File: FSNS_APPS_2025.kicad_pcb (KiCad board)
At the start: 2 copper layers, 59 parts, among them K1 PR12-12V-360-1A, Q1 NDT3055L, U1 STM32F103C8T6, U2 MCP6001-OT, U3 MCP6001-OT, U4 LM1117-Q1, U5 LM1117-Q1, U6 LM1117-Q1, U7 TCAN3404-Q1, U8 LM1117-Q1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

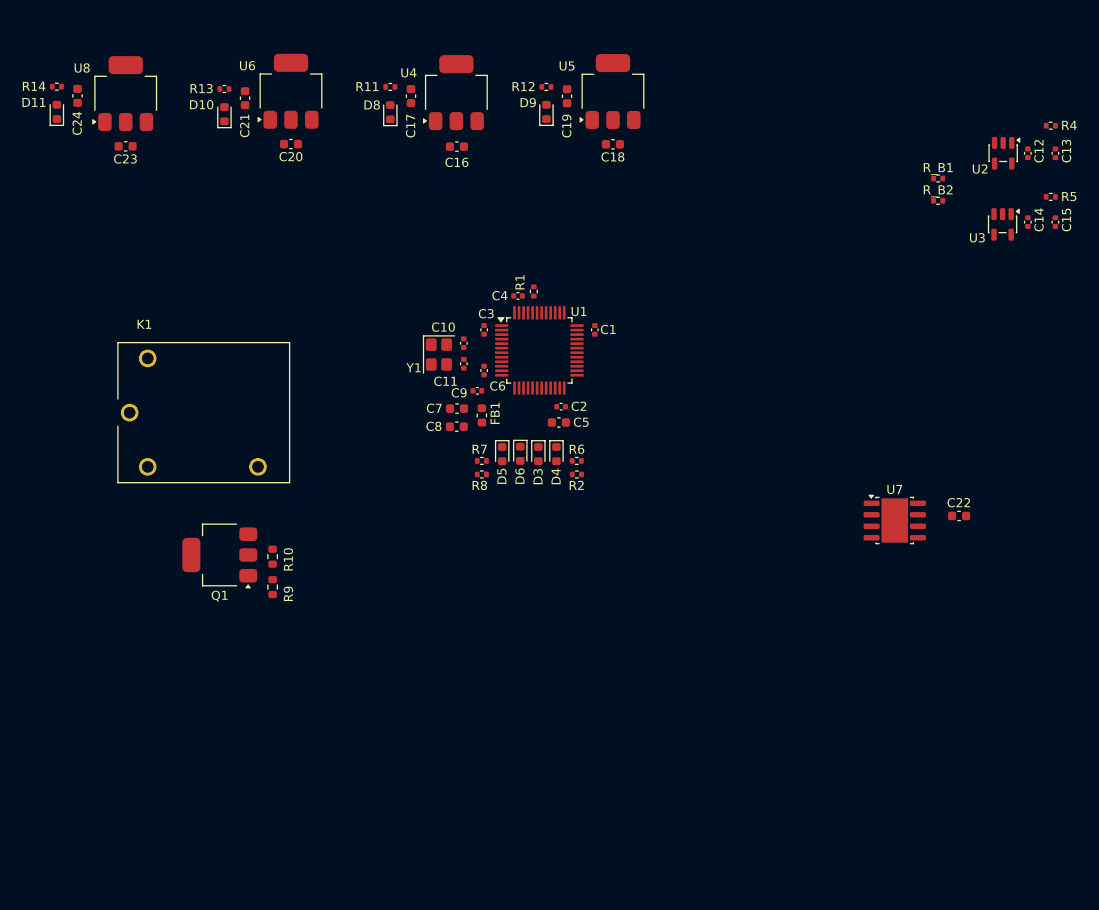
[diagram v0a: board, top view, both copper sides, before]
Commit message: Updated schematic and PCB.
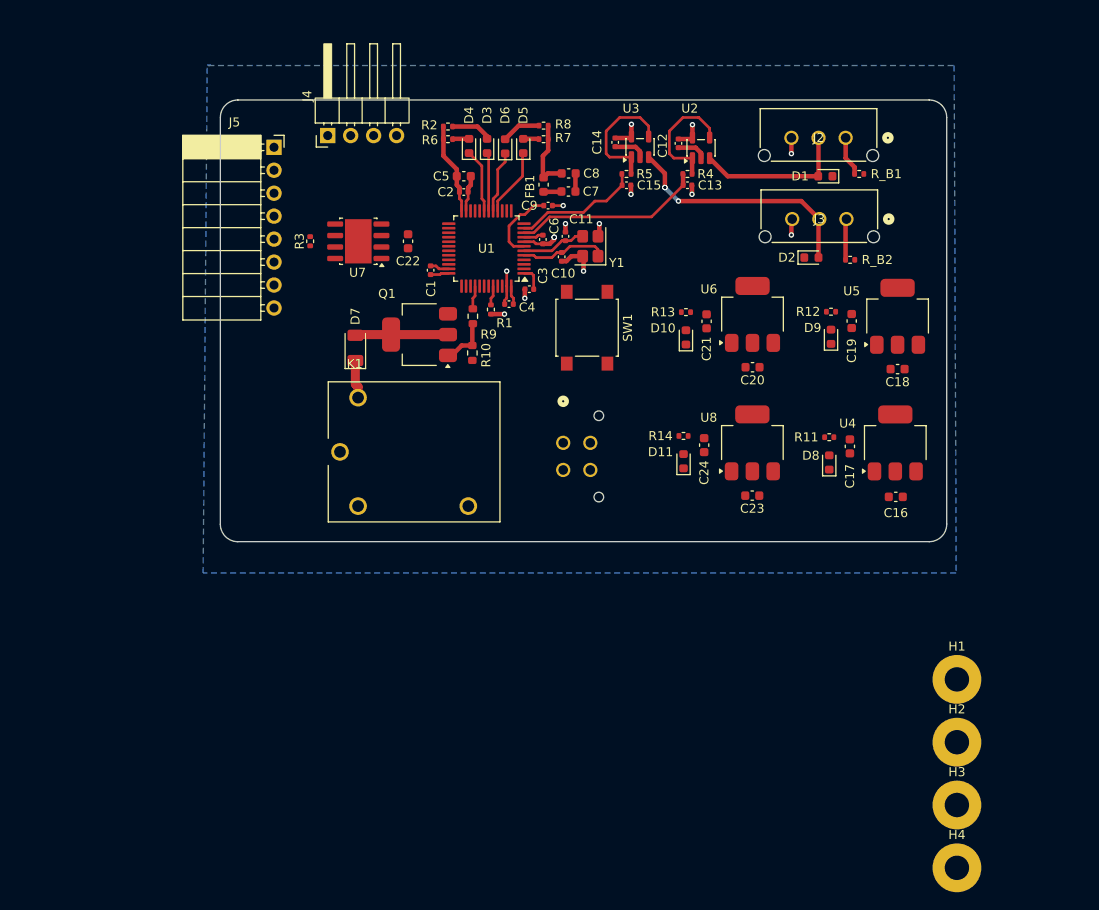
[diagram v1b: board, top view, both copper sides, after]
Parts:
- added D1: D_TVS, Diode_SMD:D_0603_1608Metric, F.Cu at (226.0, 47.5)
- added D2: D_TVS, Diode_SMD:D_0603_1608Metric, F.Cu at (224.5, 56.5)
- added D7: D, Diode_SMD:D_1206_3216Metric, F.Cu at (174.0, 66.5)
- added H1: MountingHole_Pad, MountingHole:MountingHole_2.7mm_Pad, F.Cu at (240.6, 103.2)
- added H2: MountingHole_Pad, MountingHole:MountingHole_2.7mm_Pad, F.Cu at (240.6, 110.1)
- added H3: MountingHole_Pad, MountingHole:MountingHole_2.7mm_Pad, F.Cu at (240.6, 117.1)
- added H4: MountingHole_Pad, MountingHole:MountingHole_2.7mm_Pad, F.Cu at (240.6, 124.0)
- added J1: Conn_01x04_Pin, MOLEX Micro-Fit 3.0 43045:CONN_SD-43045-005_04_MOL, B.Cu at (197.0, 77.0)
- added J2: Conn_01x03_Pin, MOLEX Micro-Fit 3.0 43045:CONN_SD-43650-006_03_MOL, F.Cu at (228.2, 43.2)
- added J3: Conn_01x03_Pin, MOLEX Micro-Fit 3.0 43045:CONN_SD-43650-006_03_MOL, F.Cu at (228.3, 52.2)
- added J4: Conn_01x04_Pin, Connector_PinHeader_2.54mm:PinHeader_1x04_P2.54mm_Horizontal, F.Cu at (170.9, 43.0)
- added J5: Conn_01x08_Pin, Connector_PinSocket_2.54mm:PinSocket_1x08_P2.54mm_Horizontal, F.Cu at (165.0, 44.3)
- added R3: 120R, Resistor_SMD:R_0402_1005Metric, F.Cu at (169.0, 54.7)
- added SW1: SW_Push, Button_Switch_SMD:SW_SPST_B3S-1000, F.Cu at (199.6, 64.3)
- moved C23 79.4 mm to (217.9, 82.8)
- moved C24 79.4 mm to (212.6, 77.3)
- moved R14 79.4 mm to (210.3, 76.2)
- moved D11 79.4 mm to (210.3, 79.0)
- moved U8 79.4 mm to (217.9, 77.0)
- moved C22 68.1 mm to (179.8, 54.7), turned to -90 degrees
- moved U7 66.9 mm to (174.3, 54.7), turned to 180 degrees
- moved C16 62.1 mm to (233.8, 83.0)
- moved C17 62.1 mm to (228.7, 77.4)
- moved D8 62.1 mm to (226.4, 79.2)
- moved R11 62.1 mm to (226.4, 76.4)
- moved U4 62.1 mm to (233.7, 77.0)
- moved C20 56.7 mm to (217.9, 68.6)
- moved U6 56.7 mm to (217.9, 62.8)
- moved C21 56.7 mm to (212.9, 63.6)
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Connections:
- net APPS1_OUT renamed /APPS1_OUT
- net APPS2_OUT renamed /APPS2_OUT
- K1 pad COM: unconnected-(K1-PadCOM) -> /APPS_SDC_IN
- K1 pad NO: unconnected-(K1-PadNO) -> /APPS_SDC_OUT
- U1 pad 25: unconnected-(U1-PB12-Pad25) -> /PB12
- U1 pad 26: unconnected-(U1-PB13-Pad26) -> /PB13
- U1 pad 27: unconnected-(U1-PB14-Pad27) -> /PB14
- U1 pad 28: unconnected-(U1-PB15-Pad28) -> /PB15
- U1 pad 29: unconnected-(U1-PA8-Pad29) -> /PA8
- U1 pad 30: unconnected-(U1-PA9-Pad30) -> /PA9
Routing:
- net GND: track 0.00 -> 38.0 mm, vias 0 -> 15
- net /POT2: track 0.00 -> 27.4 mm, vias 0 -> 3
- net +3.3V: track 0.00 -> 25.2 mm
- net /APPS1_OUT: track 0.00 -> 21.0 mm
- net /POT1: track 0.00 -> 17.1 mm
- net Net-(U3--): track 0.00 -> 14.2 mm
- net /APPS2_OUT: track 0.00 -> 14.1 mm
- net Net-(U2--): track 0.00 -> 14.0 mm
- net +3.3VA: track 0.00 -> 11.1 mm
- net Net-(D7-A): track 0.00 -> 10.3 mm
- net /OSC_IN: track 0.00 -> 9.70 mm
- net /NRST: track 0.00 -> 8.40 mm
- net /LED_DBG_3: track 0.00 -> 7.57 mm
- net /OSC_OUT: track 0.00 -> 7.15 mm
- net /LED_DBG_2: track 0.00 -> 7.09 mm
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- added copper zone on B.Cu, net GND
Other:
- board outline added: 80.4 x 48.9 mm

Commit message: Schematic and PCB v0.1
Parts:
- moved H4 117.7 mm to (160.0, 38.2)
- moved H3 85.6 mm to (160.0, 88.2)
- moved H2 71.9 mm to (239.0, 38.2)
- moved C16 38.5 mm to (195.8, 77.0), turned to -90 degrees
- moved J1 38.0 mm to (235.0, 78.2), turned to 180 degrees
- moved J4 36.6 mm to (158.9, 77.6), turned to 180 degrees
- moved U4 33.0 mm to (200.7, 77.4), turned to -90 degrees
- moved C17 23.0 mm to (205.8, 77.0), turned to 90 degrees
- moved D11 17.8 mm to (227.7, 75.0), turned to -90 degrees
- moved R14 17.2 mm to (227.4, 77.5), turned to 180 degrees
- moved D8 17.1 mm to (209.8, 75.2), turned to -90 degrees
- moved R11 17.0 mm to (209.5, 77.8), turned to 180 degrees
- moved H1 15.0 mm to (239.0, 88.2)
- moved C24 11.7 mm to (224.3, 76.7), turned to 90 degrees
- moved U7 10.3 mm to (166.3, 61.1)
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- renumbered D5 to PA6, D6 to PA7, D3 to PB0, D4 to PB1
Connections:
- J5 pad 1: /PB15 -> /PB12
- J5 pad 2: /PB14 -> /PB13
- J5 pad 3: /PB13 -> /PB14
- J5 pad 4: /PB12 -> /PB15
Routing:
- net +3.3V: track 25.2 -> 155.4 mm, vias 0 -> 4
- net GND: track 38.0 -> 117.1 mm, vias 15 -> 79
- net +5V: track 4.22 -> 72.6 mm, vias 0 -> 2
- net /APPS_SDC_IN: track 0.00 -> 64.9 mm
- net /APPS_SDC_OUT: track 0.00 -> 61.8 mm
- net +12V: track 0.00 -> 57.5 mm
- net Net-(D7-A): track 10.3 -> 51.7 mm
- net /SWCLK: track 0.00 -> 33.3 mm
- net /SWDIO: track 0.00 -> 31.8 mm
- net /PB12: track 0.00 -> 28.0 mm
- net /PB13: track 0.00 -> 27.4 mm
- net /PA9: track 0.00 -> 27.1 mm
- net /PB14: track 0.00 -> 26.4 mm
- net /PA8: track 0.00 -> 26.2 mm
- net /PB15: track 0.00 -> 25.5 mm
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- added copper zone on F.Cu, net +12V
- added copper zone on F.Cu, net +3.3V
- added copper zone on F.Cu, net +3.3V_POT1
- added copper zone on F.Cu, net +3.3V_POT2
- added copper zone on F.Cu, net +5V
- added copper zone on F.Cu, net GND
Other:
- board size 80.4 x 48.9 mm -> 89 x 60 mm
- board text added: "+3.3V"
- board text added: "+5V"
- board text added: "APPS 0.1 FSNS P. Nuzdic"
- board text added: "GND +12V SDC SDC"
- board text added: "GND POT PWR"
- board text added: "GND SWDIO SWCLK +3.3V"
- board text added: "PB12 PB13 PB14 PB15 PA8 PA9 CANL CANH"
